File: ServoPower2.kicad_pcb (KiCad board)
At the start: 2 copper layers, 26 x 57.2 mm, 16 parts, among them J1 Conn_01x03, J10 Conn_01x03, J11 Conn_01x03, J12 Conn_01x03, J13 Conn_01x02, J14 Conn_01x02, J15 Conn_01x02, J2 Conn_01x03, J3 Conn_01x03, J4 Conn_01x03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

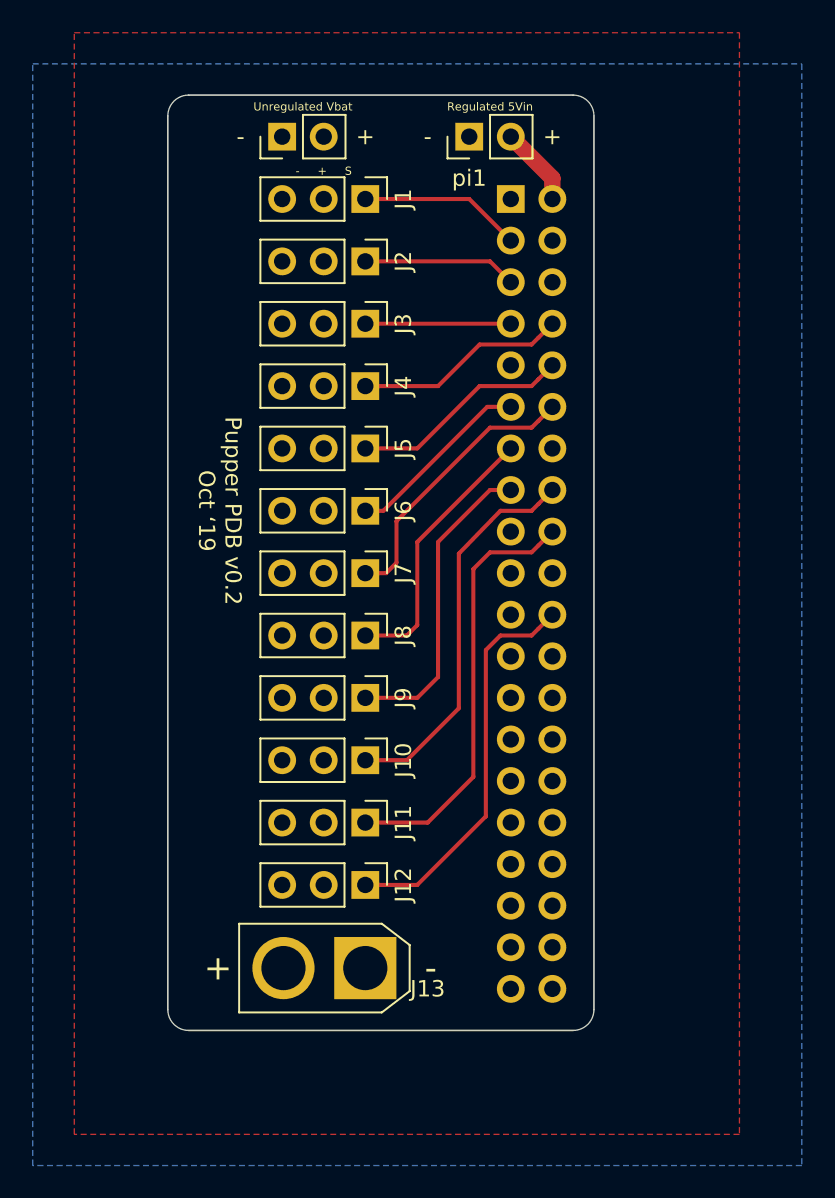
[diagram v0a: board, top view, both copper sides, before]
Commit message: rearrange pins to easier soldering
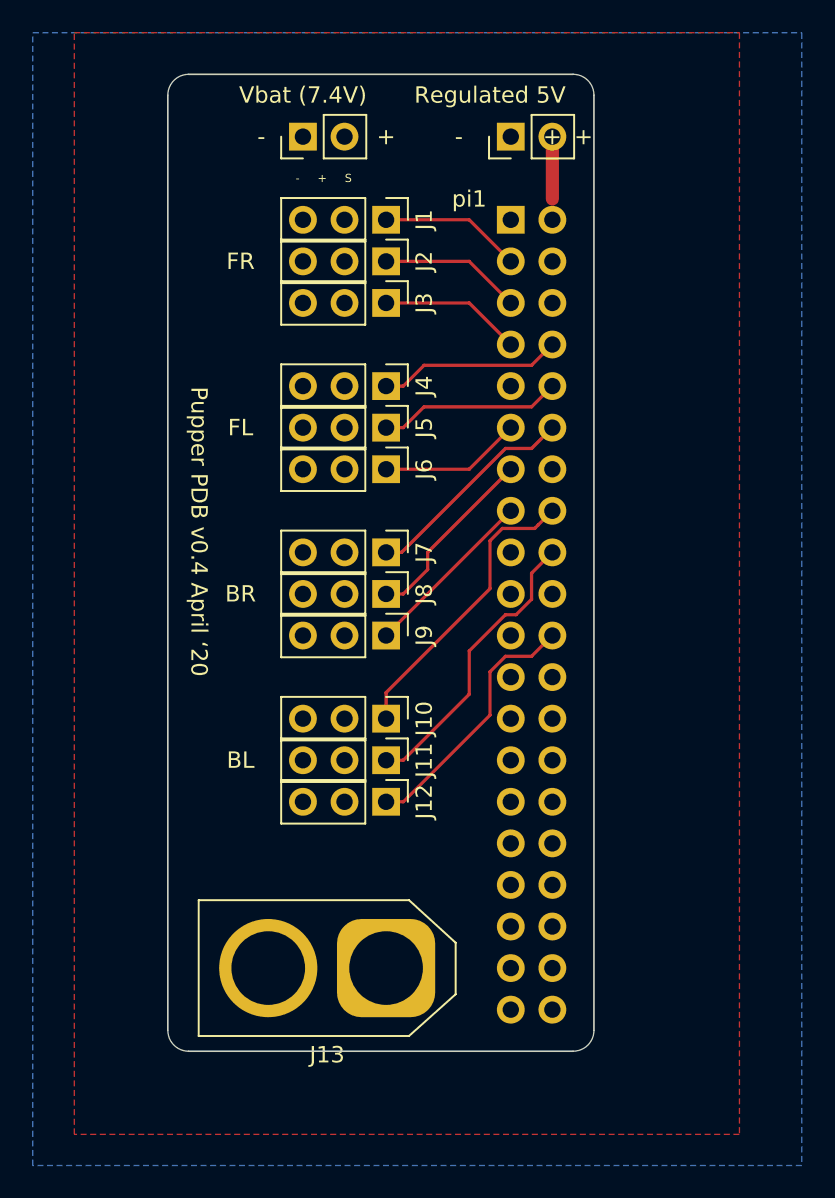
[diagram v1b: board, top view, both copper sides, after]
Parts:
- J13: footprint Connector_AMASS:AMASS_XT30U-M_1x02_P5.0mm_Vertical -> Connector_AMASS:AMASS_XT60-M_1x02_P7.20mm_Vertical
- moved J12 5.24 mm to (157.5, 104.1)
- moved J11 4.02 mm to (157.5, 101.6)
- moved J9 4.02 mm to (157.5, 94.0)
- moved J6 2.84 mm to (157.5, 83.8)
- moved J8 2.84 mm to (157.5, 91.4)
- moved J10 2.84 mm to (157.5, 99.1)
- moved J15 2.54 mm to (165.1, 63.5)
- moved J3 1.80 mm to (157.5, 73.7)
- moved J1 1.80 mm to (157.5, 68.6)
- moved J5 1.80 mm to (157.5, 81.3)
- moved J7 1.80 mm to (157.5, 88.9)
- moved J14 1.27 mm to (152.4, 63.5)
- moved pi1 1.27 mm to (165.1, 68.6)
- moved J13 1.27 mm to (157.5, 114.3)
- moved J2 1.27 mm to (157.5, 71.1)
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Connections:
- pi1 pad 1: Net-(pi1-Pad1) -> (no net)
- pi1 pad 17: Net-(pi1-Pad17) -> (no net)
- pi1 pad 19: Net-(pi1-Pad19) -> (no net)
- pi1 pad 21: Net-(pi1-Pad21) -> (no net)
- pi1 pad 23: Net-(pi1-Pad23) -> (no net)
- pi1 pad 24: Net-(pi1-Pad24) -> (no net)
- pi1 pad 26: Net-(pi1-Pad26) -> (no net)
- pi1 pad 27: Net-(pi1-Pad27) -> (no net)
- pi1 pad 28: Net-(pi1-Pad28) -> (no net)
- pi1 pad 29: Net-(pi1-Pad29) -> (no net)
- pi1 pad 31: Net-(pi1-Pad31) -> (no net)
- pi1 pad 32: Net-(pi1-Pad32) -> (no net)
- pi1 pad 33: Net-(pi1-Pad33) -> (no net)
- pi1 pad 35: Net-(pi1-Pad35) -> (no net)
- pi1 pad 36: Net-(pi1-Pad36) -> (no net)
- pi1 pad 37: Net-(pi1-Pad37) -> (no net)
- pi1 pad 38: Net-(pi1-Pad38) -> (no net)
- pi1 pad 4: Net-(pi1-Pad4) -> (no net)
- pi1 pad 40: Net-(pi1-Pad40) -> (no net)
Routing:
- net /S42: track 26.2 -> 17.9 mm
- net /S43: track 24.2 -> 15.9 mm
- net /S33: track 19.0 -> 10.8 mm
- net /S41: track 23.8 -> 18.1 mm
- net /S32: track 16.6 -> 11.4 mm
- net /S31: track 17.1 -> 13.3 mm
- net /S23: track 11.5 -> 8.67 mm
- net /S22: track 13.5 -> 11.2 mm
- net /S21: track 13.0 -> 11.2 mm
- net /S11: track 9.94 -> 8.67 mm
- net +5V: track 4.86 -> 3.81 mm
- net /S12: track 9.42 -> 8.67 mm
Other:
- board size 26 x 57.2 mm -> 26 x 59.7 mm
- net class Power: trace_width 1 -> 0.8
- board text added: "BL"
- board text added: "BR"
- board text added: "FL"
- board text added: "FR"
- board text added: "Pupper PDB v0.4 April ‘20"
- board text added: "Regulated 5V"
- board text added: "Vbat (7.4V)"
- board text removed: "Pupper PDB v0.2 Oct ‘19"
- board text removed: "Regulated 5Vin"
- board text removed: "Unregulated Vbat"

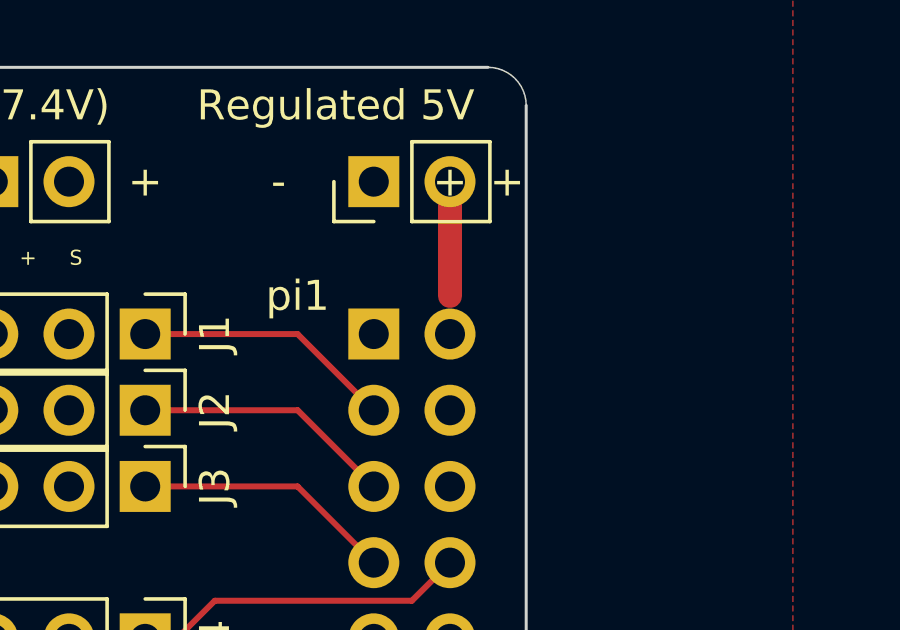
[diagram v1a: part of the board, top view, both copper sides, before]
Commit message: fix incomplete track
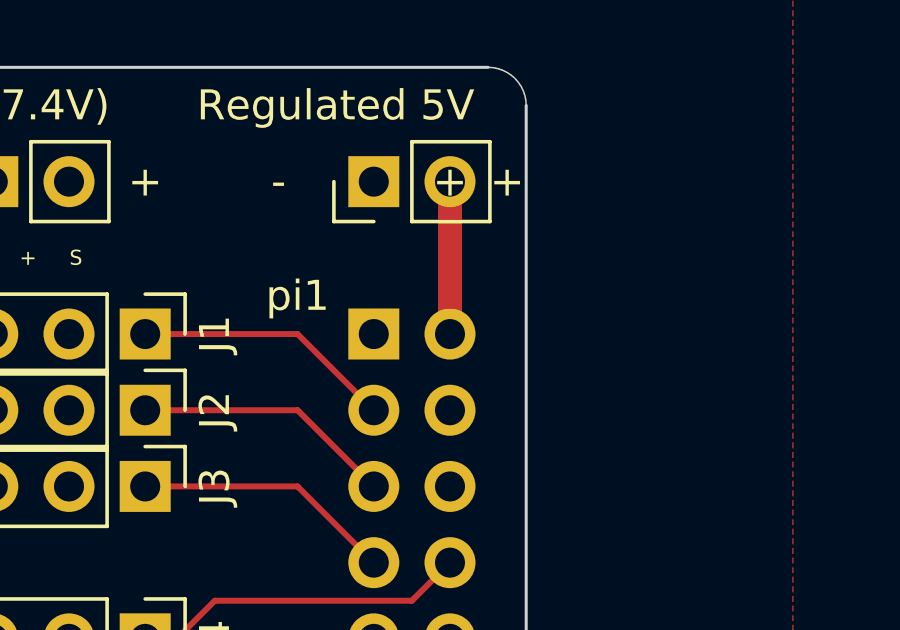
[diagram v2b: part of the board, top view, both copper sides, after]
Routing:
- net +5V: track 3.81 -> 5.08 mm
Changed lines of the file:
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@@
     (thickness 1.6)
     (drawings 21)
-    (tracks 47)
+    (tracks 48)
     (zones 0)
     (modules 16)
@@
     (add_net /S43)
     (add_net GND)
-    (add_net "Net-(pi1-Pad1)")
-    (add_net "Net-(pi1-Pad17)")
-    (add_net "Net-(pi1-Pad19)")
-    (add_net "Net-(pi1-Pad21)")
-    (add_net "Net-(pi1-Pad23)")
-    (add_net "Net-(pi1-Pad24)")
-    (add_net "Net-(pi1-Pad26)")
-    (add_net "Net-(pi1-Pad27)")
-    (add_net "Net-(pi1-Pad28)")
-    (add_net "Net-(pi1-Pad29)")
-    (add_net "Net-(pi1-Pad31)")
-    (add_net "Net-(pi1-Pad32)")
-    (add_net "Net-(pi1-Pad33)")
-    (add_net "Net-(pi1-Pad35)")
-    (add_net "Net-(pi1-Pad36)")
-    (add_net "Net-(pi1-Pad37)")
-    (add_net "Net-(pi1-Pad38)")
-    (add_net "Net-(pi1-Pad4)")
-    (add_net "Net-(pi1-Pad40)")
     (add_net VDD)
   )
@@
   (segment (start 157.48 71.12) (end 162.56 71.12) (width 0.2) (layer F.Cu) (net 14))
   (segment (start 167.64 67.31) (end 167.64 63.5) (width 0.8) (layer F.Cu) (net 15) (status 30))
+  (segment (start 167.64 67.31) (end 167.64 68.58) (width 0.8) (layer F.Cu) (net 15))
   (zone (net 1) (net_name VDD) (layer F.Cu) (hatch edge 0.508)
     (connect_pads (clearance 0.127))
